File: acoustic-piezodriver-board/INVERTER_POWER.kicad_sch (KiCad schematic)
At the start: 58 parts, among them Q501 AO3400A, Q502 AO3400A, U501 NCE6005AS, U502 LM3478MM, U503 NCE6005AS, U504 LM3478MM

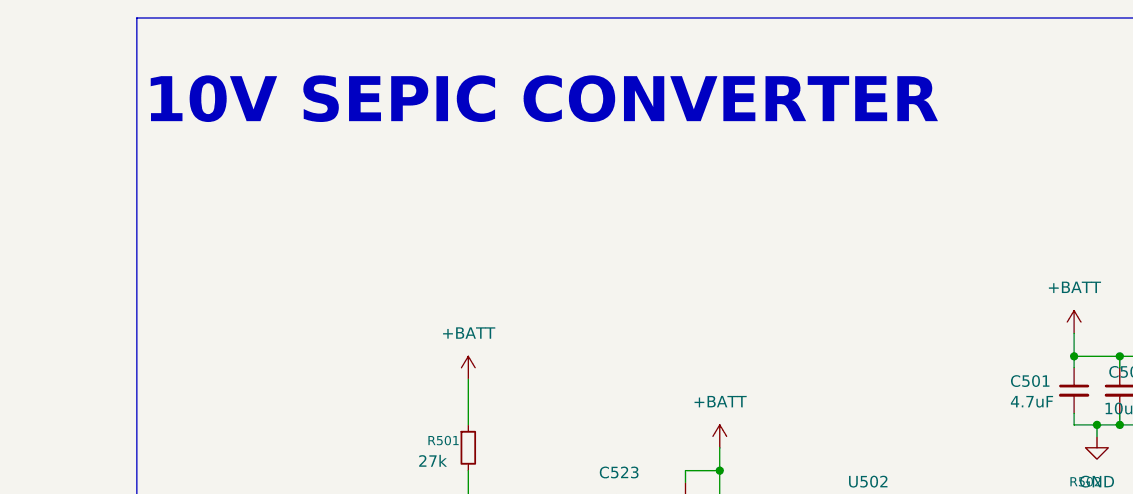
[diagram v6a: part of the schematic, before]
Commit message: fixed erc and drc errors completely, added 3d models for connectors, finished DFM (next) create gerbers, check
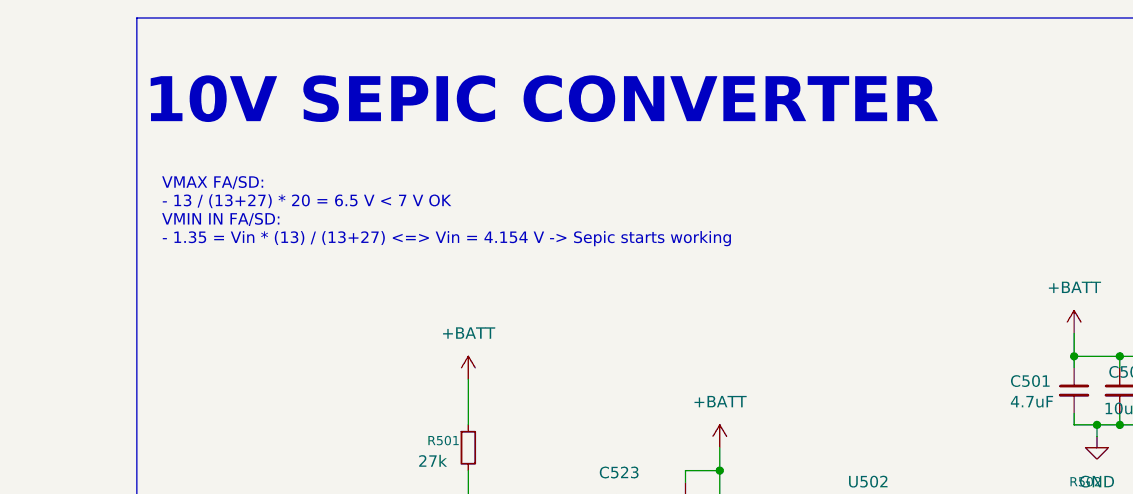
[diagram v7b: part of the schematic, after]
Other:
- note added: "VMAX FA/SD: - 13 / (13+27) * 20 = 6.5 V < 7 V OK VMIN IN FA/SD: - 1.35 = Vin * (13) / (13+27) <=> Vin = 4.154 V -> Sepic starts working"
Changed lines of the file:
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@@
+		)
+	)
+	(text "VMAX FA/SD:\n- 13 / (13+27) * 20 = 6.5 V < 7 V OK\nVMIN IN FA/SD:\n- 1.35 = Vin * (13) / (13+27) <=> Vin = 4.154 V -> Sepic starts working"
+		(exclude_from_sim no)
+		(at 203.454 42.418 0)
+		(effects
+			(font
+				(size 1.27 1.27)
+			)
+			(justify left)
 		)
 	)

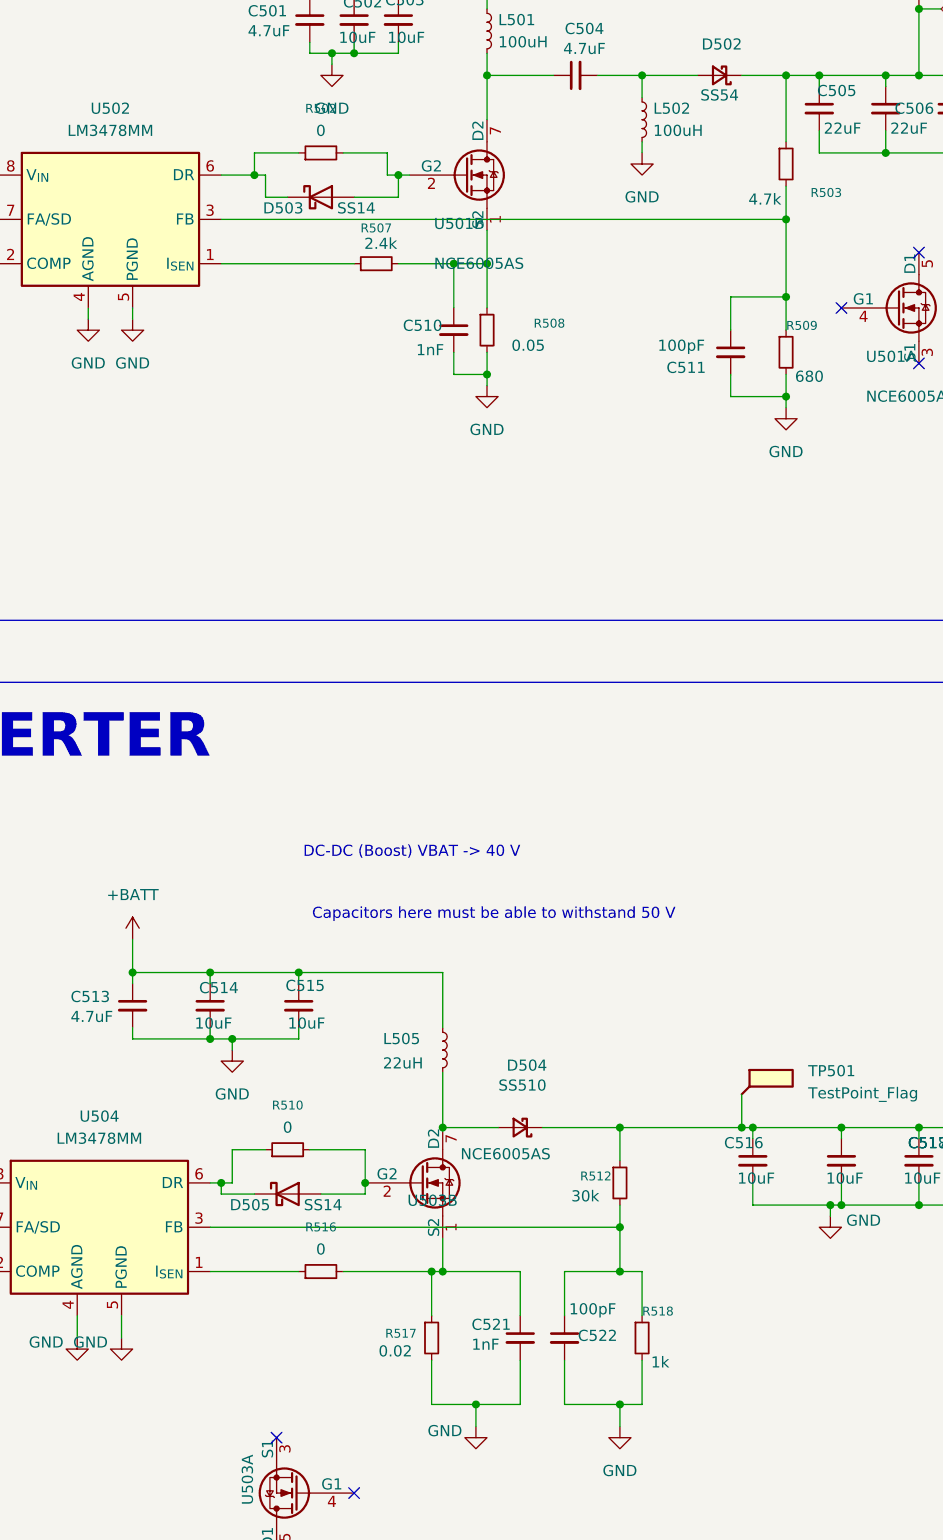
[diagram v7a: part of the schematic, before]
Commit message: added testpoints on fb and isense pins (next) double-check schematic and order
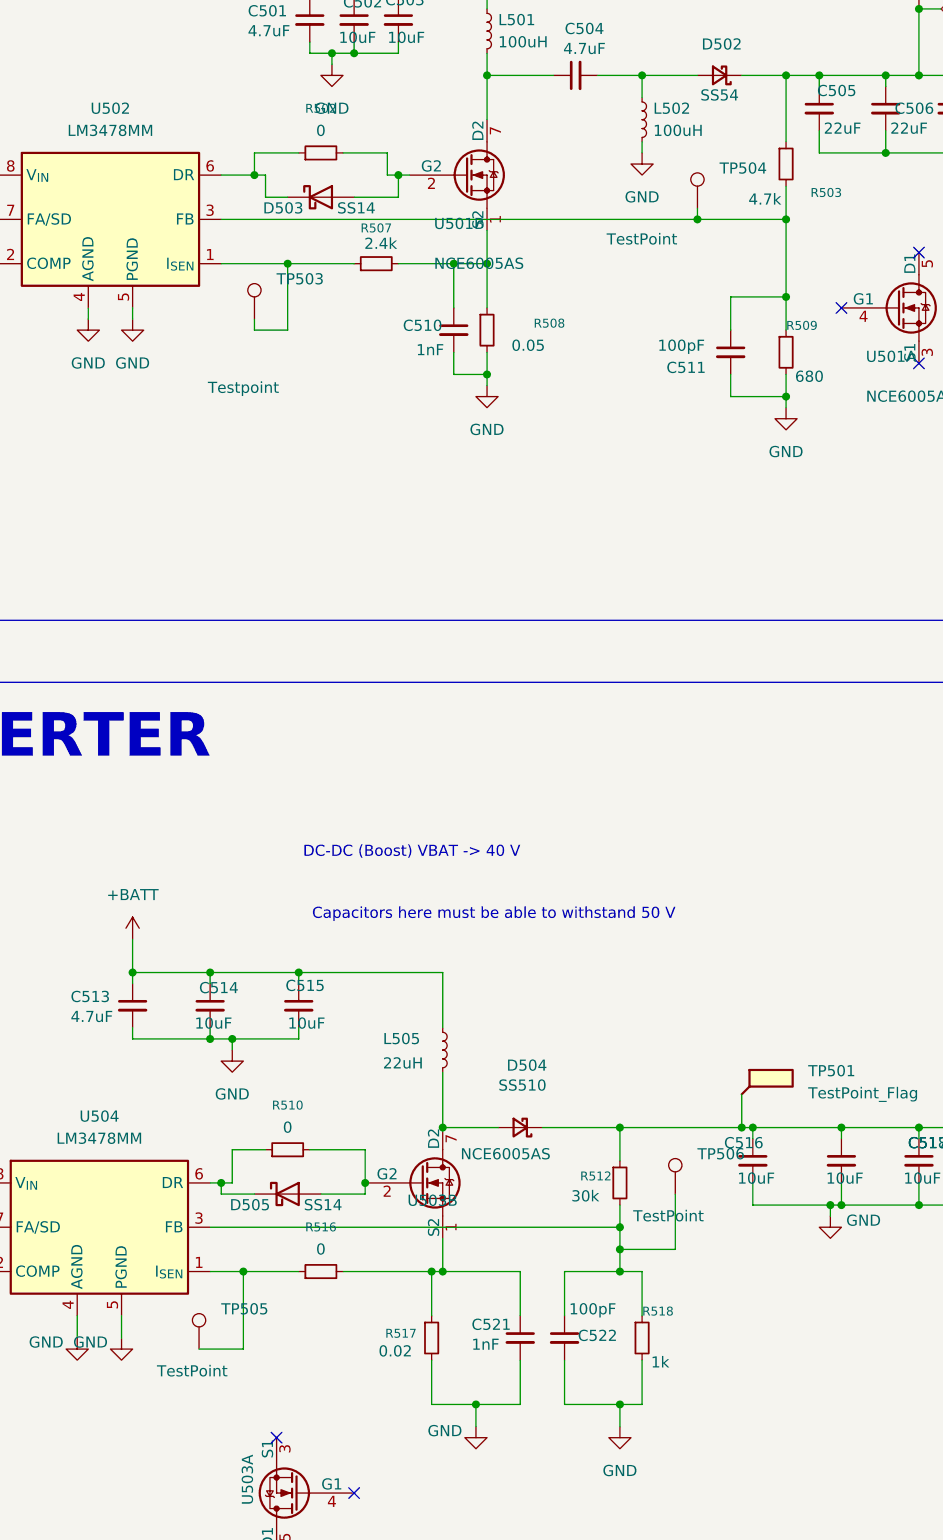
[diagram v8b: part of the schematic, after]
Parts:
- added TP503: Testpoint, TestPoint:TestPoint_Pad_D1.0mm, symbol iw-misc:TestPoint_0.25mm
- added TP504, TP505, TP506: TestPoint, TestPoint:TestPoint_Pad_D1.0mm, symbol iw-misc:TestPoint_0.25mm
- C501, C504, C513: LCSC Part Number (none) -> C29823; LPN C29823 -> (none); MPN 1206B475K500NT -> (none); Manufacturing Part Number (none) -> 1206B475K500NT
- C502, C503, C514, C515, C516, C517, C518, C519: LCSC Part Number (none) -> C440198; LPN C440198 -> (none); MPN GRM21BR61H106KE43L -> (none); Manufacturing Part Number (none) -> GRM21BR61H106KE43L
- C505, C506, C507, C508: LCSC Part Number (none) -> C45783; LPN C45783 -> (none); MPN CL21A226MAQNNNE -> (none); Manufacturing Part Number (none) -> CL21A226MAQNNNE
- C509: LCSC Part Number (none) -> C5378; LPN C5378 -> (none); MPN CL21B224KBFNNNE -> (none); Manufacturing Part Number (none) -> CL21B224KBFNNNE
- C510, C521: LCSC Part Number (none) -> C1523; LPN C1523 -> (none); MPN 0402B102K500NT -> (none); Manufacturing Part Number (none) -> 0402B102K500NT
- C511, C522: LCSC Part Number (none) -> C1546; LPN C1546 -> (none); MPN 0402CG101J500NT -> (none); Manufacturing Part Number (none) -> 0402CG101J500NT
- C512: LCSC Part Number (none) -> C1663; LPN C1663 -> (none); MPN CL10C330JB8NNNC -> (none); Manufacturing Part Number (none) -> CL10C330JB8NNNC
- C520: LCSC Part Number (none) -> C14663; LPN C14663 -> (none); MPN CC0603KRX7R9BB104 -> (none); Manufacturing Part Number (none) -> CC0603KRX7R9BB104
- C523, C524: LCSC Part Number (none) -> C307331; LPN C307331 -> (none); MPN CL05B104KB54PNC -> (none); Manufacturing Part Number (none) -> CL05B104KB54PNC
- D501, D504: LCSC Part Number (none) -> C65010; LPN C65010 -> (none); MPN SS510 -> (none); Manufacturing Part Number (none) -> SS510
- D502: LCSC Part Number (none) -> C22452; LPN C22452 -> (none); MPN SS54 -> (none); Manufacturing Part Number (none) -> SS54
- D503, D505: LCSC Part Number (none) -> C2480; LPN C2480 -> (none); MPN SS14 -> (none); Manufacturing Part Number (none) -> SS14
- L501, L502: LCSC Part Number (none) -> C5273830; LPN C5273830 -> (none); MPN PSPMAA1050H-101M-ANP -> (none); Manufacturing Part Number (none) -> PSPMAA1050H-101M-ANP
- L505: LCSC Part Number (none) -> C2453841; LPN C2453841 -> (none); MPN PA4343.223NLT -> (none); Manufacturing Part Number (none) -> PA4343.223NLT
- Q501, Q502: LCSC Part Number (none) -> C20917; LPN C20917 -> (none); MPN AO3400A -> (none); Manufacturing Part Number (none) -> AO3400A
- R501, R511: LCSC Part Number (none) -> C22967; LPN C22967 -> (none); MPN 0603WAF2702T5E -> (none); Manufacturing Part Number (none) -> 0603WAF2702T5E
- R502, R510, R516: LCSC Part Number (none) -> C15402; LPN C15402 -> (none); MPN 0603WAJ0000T5E -> (none); Manufacturing Part Number (none) -> 0603WAJ0000T5E
- R503: LCSC Part Number (none) -> C23162; LPN C23162 -> (none); MPN 0603WAF4701T5E -> (none); Manufacturing Part Number (none) -> 0603WAF4701T5E
- R504, R513: LCSC Part Number (none) -> C22797; LPN C22797 -> (none); MPN 0603WAF1302T5E -> (none); Manufacturing Part Number (none) -> 0603WAF1302T5E
- R505, R514, R515: LCSC Part Number (none) -> C23153; LPN C23153 -> (none); MPN 0603WAF3902T5E -> (none); Manufacturing Part Number (none) -> 0603WAF3902T5E
- R506: LCSC Part Number (none) -> C13167; LPN C13167 -> (none); MPN 0603WAF2701T5E -> (none); Manufacturing Part Number (none) -> 0603WAF2701T5E
- R507: LCSC Part Number (none) -> C17526; LPN C17526 -> (none); MPN 0805W8F2401T5E -> (none); Manufacturing Part Number (none) -> 0805W8F2401T5E
- R508: LCSC Part Number (none) -> C127691; LPN C127691 -> (none); MPN 1206W3F500MT5E -> (none); Manufacturing Part Number (none) -> 1206W3F500MT5E
- R509: LCSC Part Number (none) -> C23228; LPN C23228 -> (none); MPN 0603WAF6800T5E -> (none); Manufacturing Part Number (none) -> 0603WAF6800T5E
- R512: LCSC Part Number (none) -> C22984; LPN C22984 -> (none); MPN 0603WAF3002T5E -> (none); Manufacturing Part Number (none) -> 0603WAF3002T5E
- R517: LCSC Part Number (none) -> C2765435; LPN C2765435 -> (none); MPN 1206W3F200MT5E -> (none); Manufacturing Part Number (none) -> 1206W3F200MT5E
- R518: LCSC Part Number (none) -> C21190; LPN C21190 -> (none); MPN 0603WAF1001T5E -> (none); Manufacturing Part Number (none) -> 0603WAF1001T5E
- TP501, TP502: now left out of the parts list
- U501, U503: LCSC Part Number (none) -> C126151; LPN C126151 -> (none); MPN NCE6005AS -> (none); Manufacturing Part Number (none) -> NCE6005AS
- U502, U504: LCSC Part Number (none) -> C404045; LPN C404045 -> (none); MPN LM3478MMX/NOPB -> (none); Manufacturing Part Number (none) -> LM3478MMX/NOPB
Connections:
- net at R516.1, U504.1 (I_{SEN}): now also TP505.1
- net at C522.1, R512.2, R518.1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: now also TP506.1
- net at R507.1, U502.1 (I_{SEN}): now also TP503.1
- net at C511.1, R503.2, R509.1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: now also TP504.1
